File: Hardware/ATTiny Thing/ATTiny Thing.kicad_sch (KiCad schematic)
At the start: 9 parts, among them J1 JST_SH_BM048, J2 UPDI Connection, U1 ATtiny1617

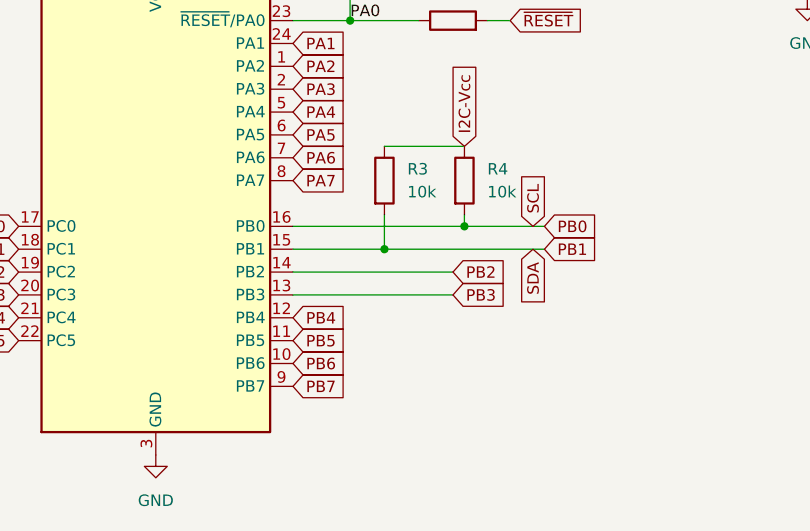
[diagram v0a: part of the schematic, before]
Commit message: Found the male XT30 & improved the XT30 board
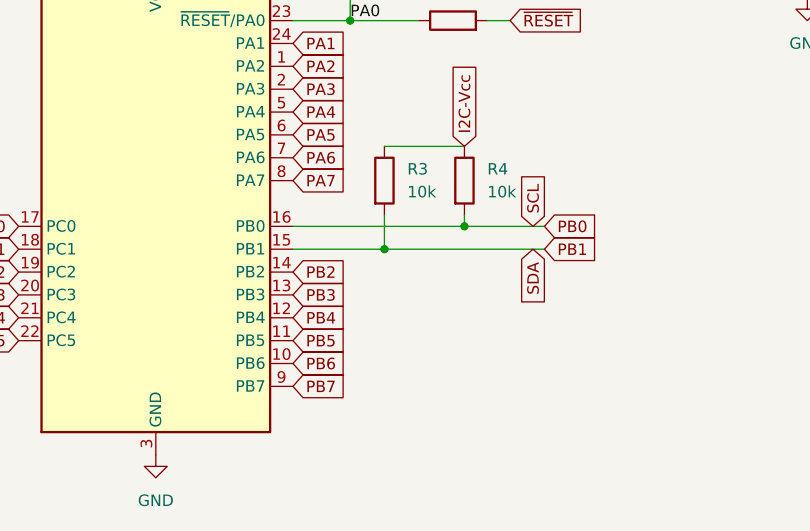
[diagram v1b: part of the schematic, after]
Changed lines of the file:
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@@
-    (stroke (width 0) (type default) (color 0 0 0 0))
-  )
-  (wire (pts (xy 165.1 85.09) (xy 182.88 85.09))
     (stroke (width 0) (type default) (color 0 0 0 0))
   )
   (wire (pts (xy 149.86 41.91) (xy 149.86 49.53))
-    (stroke (width 0) (type default) (color 0 0 0 0))
-  )
-  (wire (pts (xy 165.1 87.63) (xy 182.88 87.63))
     (stroke (width 0) (type default) (color 0 0 0 0))
   )
@@
     )
   )
-  (global_label "PB2" (shape input) (at 182.88 85.09 0) (fields_autoplaced)
+  (global_label "PB2" (shape input) (at 165.1 85.09 0) (fields_autoplaced)
     (effects (font (size 1.27 1.27)) (justify left))
-    (property "Intersheet References" "${INTERSHEET_REFS}" (id 0) (at 188.9537 85.0106 0)
+    (property "Intersheet References" "${INTERSHEET_REFS}" (id 0) (at 171.1737 85.0106 0)
       (effects (font (size 1.27 1.27)) (justify left) hide)
     )
@@
     )
   )
-  (global_label "PB3" (shape input) (at 182.88 87.63 0) (fields_autoplaced)
+  (global_label "PB3" (shape input) (at 165.1 87.63 0) (fields_autoplaced)
     (effects (font (size 1.27 1.27)) (justify left))
-    (property "Intersheet References" "${INTERSHEET_REFS}" (id 0) (at 188.9537 87.5506 0)
+    (property "Intersheet References" "${INTERSHEET_REFS}" (id 0) (at 171.1737 87.5506 0)
       (effects (font (size 1.27 1.27)) (justify left) hide)
     )
